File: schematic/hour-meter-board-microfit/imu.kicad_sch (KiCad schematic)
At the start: 8 parts, among them U601 MPU-6500, U602 LIS3MDLTR

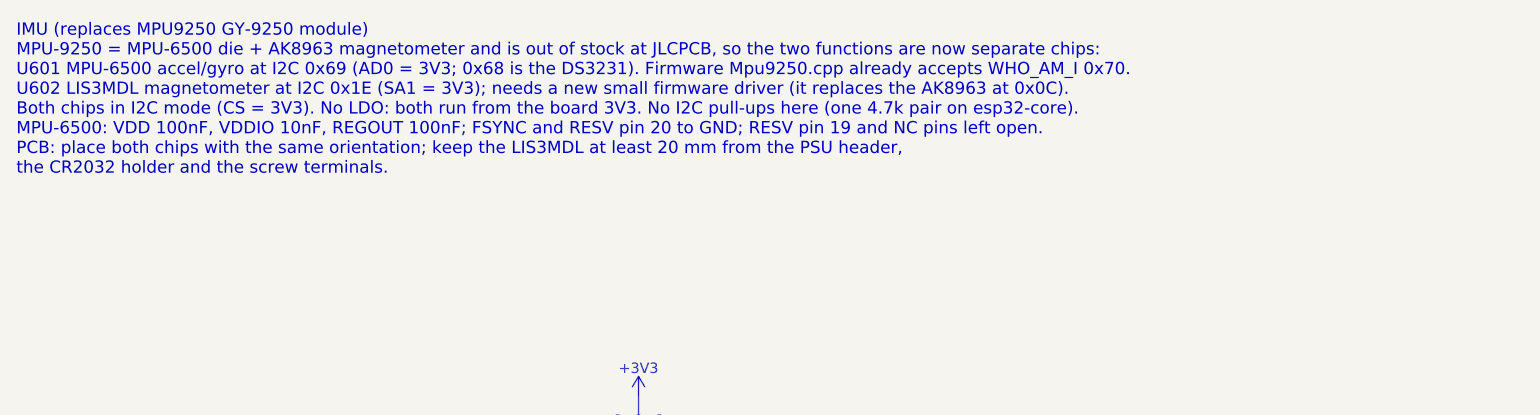
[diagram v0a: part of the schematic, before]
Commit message: feat(pcb): wire the Micro-Fit board's field I/O through one J1 harness
- New Harness sheet: J1 Molex Micro-Fit 3.0 2x7 right-angle header
  (43045-1400, LCSC C277677) replaces J101, J301, J701, J801 and J902.
- Pin order: VIN, AIN1, DOUT1, DIN1 and DIN2 sit on the back row (8-14)
  so their 0.8 mm Vehicle clearance never has to fit between two pads.
  The isolated DIN group (DIN1, DIN2 and two DIN COM pins 6/7) fills
  the pin 7/14 end, next to RS485 A/B, which are rated +/-70 V.
- J802 GPS becomes a JST GH 6-pin in the Pixhawk pinout with I2C;
  PPS moves to the TP801 solder pad.
- The J804 expansion header becomes test pads TP802-TP808; F802 and
  F902 go. J501, J702 and J703 become solder jumpers JP501, JP702-JP704.
- U501 is now the SOIC-8 AT24C256C-SSHL-T (C6482); TP101/TP102 dropped.
- Net-class patterns follow the renamed root nets; ERC shows only the
  two known IMU warnings.
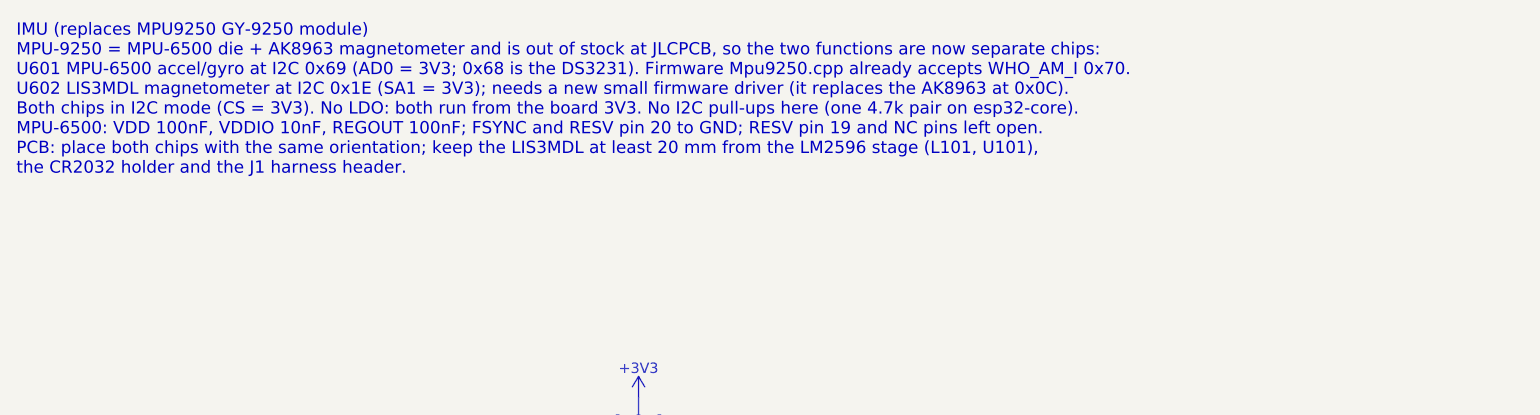
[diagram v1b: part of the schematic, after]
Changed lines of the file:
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@@
 	(generator_version "10.0")
 	(paper "A4")
-	(text "IMU (replaces MPU9250 GY-9250 module)\nMPU-9250 = MPU-6500 die + AK8963 magnetometer and is out of stock at JLCPCB, so the two functions are now separate chips:\nU601 MPU-6500 accel/gyro at I2C 0x69 (AD0 = 3V3; 0x68 is the DS3231). Firmware Mpu9250.cpp already accepts WHO_AM_I 0x70.\nU602 LIS3MDL magnetometer at I2C 0x1E (SA1 = 3V3); needs a new small firmware driver (it replaces the AK8963 at 0x0C).\nBoth chips in I2C mode (CS = 3V3). No LDO: both run from the board 3V3. No I2C pull-ups here (one 4.7k pair on esp32-core).\nMPU-6500: VDD 100nF, VDDIO 10nF, REGOUT 100nF; FSYNC and RESV pin 20 to GND; RESV pin 19 and NC pins left open.\nPCB: place both chips with the same orientation; keep the LIS3MDL at least 20 mm from the PSU header,\nthe CR2032 holder and the screw terminals."
-		(exclude_from_sim no)
-		(at 25.4 25.4 0)
-		(effects
-			(font
-				(size 1.5 1.5)
-			)
-			(justify left top)
-		)
-	)
 	(junction
 		(at 99.06 73.66)
@@
 		)
 	)
+  (text "IMU (replaces MPU9250 GY-9250 module)\nMPU-9250 = MPU-6500 die + AK8963 magnetometer and is out of stock at JLCPCB, so the two functions are now separate chips:\nU601 MPU-6500 accel/gyro at I2C 0x69 (AD0 = 3V3; 0x68 is the DS3231). Firmware Mpu9250.cpp already accepts WHO_AM_I 0x70.\nU602 LIS3MDL magnetometer at I2C 0x1E (SA1 = 3V3); needs a new small firmware driver (it replaces the AK8963 at 0x0C).\nBoth chips in I2C mode (CS = 3V3). No LDO: both run from the board 3V3. No I2C pull-ups here (one 4.7k pair on esp32-core).\nMPU-6500: VDD 100nF, VDDIO 10nF, REGOUT 100nF; FSYNC and RESV pin 20 to GND; RESV pin 19 and NC pins left open.\nPCB: place both chips with the same orientation; keep the LIS3MDL at least 20 mm from the LM2596 stage (L101, U101),\nthe CR2032 holder and the J1 harness header."
+    (at 25.4 25.4 0)
+    (effects (font (size 1.5 1.5)) (justify left top))
+  )
 	(symbol
 		(lib_id "Device:C")
